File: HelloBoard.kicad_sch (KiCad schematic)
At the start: 42 parts, among them J1 USB_B_Micro, J2 Conn_01x04_Pin, J3 Conn_01x04_Pin, J4 Conn_02x08_Top_Bottom, SW1 SW_Push, SW2 SW_Push, U1 STM32F103C8T6, U2 AMS1117-3.3, U3 TMP235A2DCKR, U4 ADXL343, Y1 16MHz

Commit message: basic placement done
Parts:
- added J5: Conn_01x02, Connector_PinHeader_2.54mm:PinHeader_1x02_P2.54mm_Vertical, symbol Connector_Generic:Conn_01x02
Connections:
- net USER_LED_K: now reaches D2.1 (K), R5.2
- net at U4.8 (INT1): now also J5.1 (Pin_1)
- net at U4.9 (INT2): now also J5.2 (Pin_2)
- net NODE_USER_BUTTON: now reaches R6.1, R7.1, SW2.2
- no-connect marks 13 -> 11
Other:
- note added: "TODO: accelerometer footprint and schematic"
- note removed: "TODO: 7 Seg footprint 74HC595 for 7 seg ?"
- moved on the sheet: SW2, U4

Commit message: حلتيته
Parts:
- D1, D2: footprint LED_SMD:LED_0201_0603Metric -> LED_SMD:LED_0603_1608Metric
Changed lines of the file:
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@@
 			)
 		)
-		(property "Footprint" "LED_SMD:LED_0201_0603Metric"
+		(property "Footprint" "LED_SMD:LED_0603_1608Metric"
 			(at 99.06 179.07 0)
 			(effects
@@
 			)
 		)
-		(property "Footprint" "LED_SMD:LED_0201_0603Metric"
+		(property "Footprint" "LED_SMD:LED_0603_1608Metric"
 			(at 53.34 137.16 0)
 			(effects

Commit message: gonna try stuff, checkpoint
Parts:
- added R10, R11, R12, R13, R14, R15, R16, R8, R9: 220, Resistor_SMD:R_0402_1005Metric, symbol Device:R
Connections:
- net 7SEG_A: now also R12.1; no longer LED1.10 (A)
- net 7SEG_B: now also R11.1; no longer LED1.9 (B)
- net 7SEG_C: now also R13.1; no longer LED1.1 (C)
- net 7SEG_D: now also R15.1; no longer LED1.4 (D)
- net 7SEG_D1_CA: now also R10.1; no longer LED1.8 (DIG1)
- net 7SEG_D2_CA: now also R9.1; no longer LED1.7 (DIG2)
- net 7SEG_E: now also R14.1; no longer LED1.3 (E)
- net 7SEG_F: now also R8.1; no longer LED1.6 (F)
- net 7SEG_G: now also R16.1; no longer LED1.5 (G)
- new net A: LED1.10 (A), R12.2
- new net B: LED1.9 (B), R11.2
- new net C: LED1.1 (C), R13.2
- new net D: LED1.4 (D), R15.2
- new net D1_CA: LED1.8 (DIG1), R10.2
- new net D2_CA: LED1.7 (DIG2), R9.2
- new net E: LED1.3 (E), R14.2
- new net F: LED1.6 (F), R8.2
- new net G: LED1.5 (G), R16.2

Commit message: minor silkscreen edits
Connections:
- net ADXL_INT1: now reaches J5.1 (Pin_1), U4.8 (INT1)
- net ADXL_INT2: now reaches J5.2 (Pin_2), U4.9 (INT2)
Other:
- moved on the sheet: J5
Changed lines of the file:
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@@
 	)
 	(rectangle
-		(start 142.24 111.76)
-		(end 220.98 163.83)
+		(start 142.24 110.49)
+		(end 222.25 163.83)
 		(stroke
 			(width 0)
@@
 	(rectangle
 		(start 181.61 78.74)
-		(end 222.25 110.49)
+		(end 222.25 109.22)
 		(stroke
 			(width 0)
@@
 	(wire
 		(pts
-			(xy 266.7 144.78) (xy 270.51 144.78)
+			(xy 266.7 144.78) (xy 274.32 144.78)
 		)
 		(stroke
@@
 	(wire
 		(pts
-			(xy 266.7 147.32) (xy 270.51 147.32)
+			(xy 266.7 147.32) (xy 274.32 147.32)
 		)
 		(stroke
@@
 		)
 	)
+	(label "ADXL_INT2"
+		(at 270.51 147.32 270)
+		(effects
+			(font
+				(size 1.27 1.27)
+			)
+			(justify right bottom)
+		)
+	)
 	(label "BOOT0"
 		(at 53.34 64.77 0)
@@
 	)
 	(label "F"
-		(at 167.64 113.03 0)
+		(at 167.64 113.03 180)
 		(effects
 			(font
 				(size 1.27 1.27)
 			)
-			(justify left bottom)
+			(justify right bottom)
 		)
 	)
@@
 		)
 	)
+	(label "ADXL_INT1"
+		(at 270.51 144.78 90)
+		(effects
+			(font
+				(size 1.27 1.27)
+			)
+			(justify left bottom)
+		)
+	)
 	(label "I2C_SCL"
 		(at 35.56 179.07 0)
@@
 		(on_board yes)
 		(dnp no)
-		(fields_autoplaced yes)
 		(property "Reference" "U4"
-			(at 269.24 138.3598 0)
+			(at 264.922 129.794 0)
 			(effects
 				(font
@@
 		)
 		(property "Value" "ADXL343"
-			(at 269.24 140.8998 0)
+			(at 264.922 132.334 0)
 			(effects
 				(font
@@
 	(symbol
 		(lib_id "Connector_Generic:Conn_01x02")
-		(at 275.59 144.78 0)
+		(at 279.4 144.78 0)
 		(unit 1)
 		(exclude_from_sim no)
@@
 		(dnp no)
 		(property "Reference" "J5"
-			(at 268.478 152.654 0)
+			(at 269.494 159.004 0)
 			(effects
 				(font
@@
 		)
 		(property "Value" "Conn_01x02"
-			(at 268.478 155.194 0)
+			(at 269.494 161.544 0)
 			(effects
 				(font
@@
 		)
 		(property "Footprint" "Connector_PinHeader_2.54mm:PinHeader_1x02_P2.54mm_Vertical"
-			(at 275.59 144.78 0)
+			(at 279.4 144.78 0)
 			(effects
 				(font
@@
 		)
 		(property "Datasheet" "~"
-			(at 275.59 144.78 0)
+			(at 279.4 144.78 0)
 			(effects
 				(font
@@
 		)
 		(property "Description" "Generic connector, single row, 01x02, script generated (kicad-library-utils/schlib/autogen/connector/)"
-			(at 275.59 144.78 0)
+			(at 279.4 144.78 0)
 			(effects
 				(font

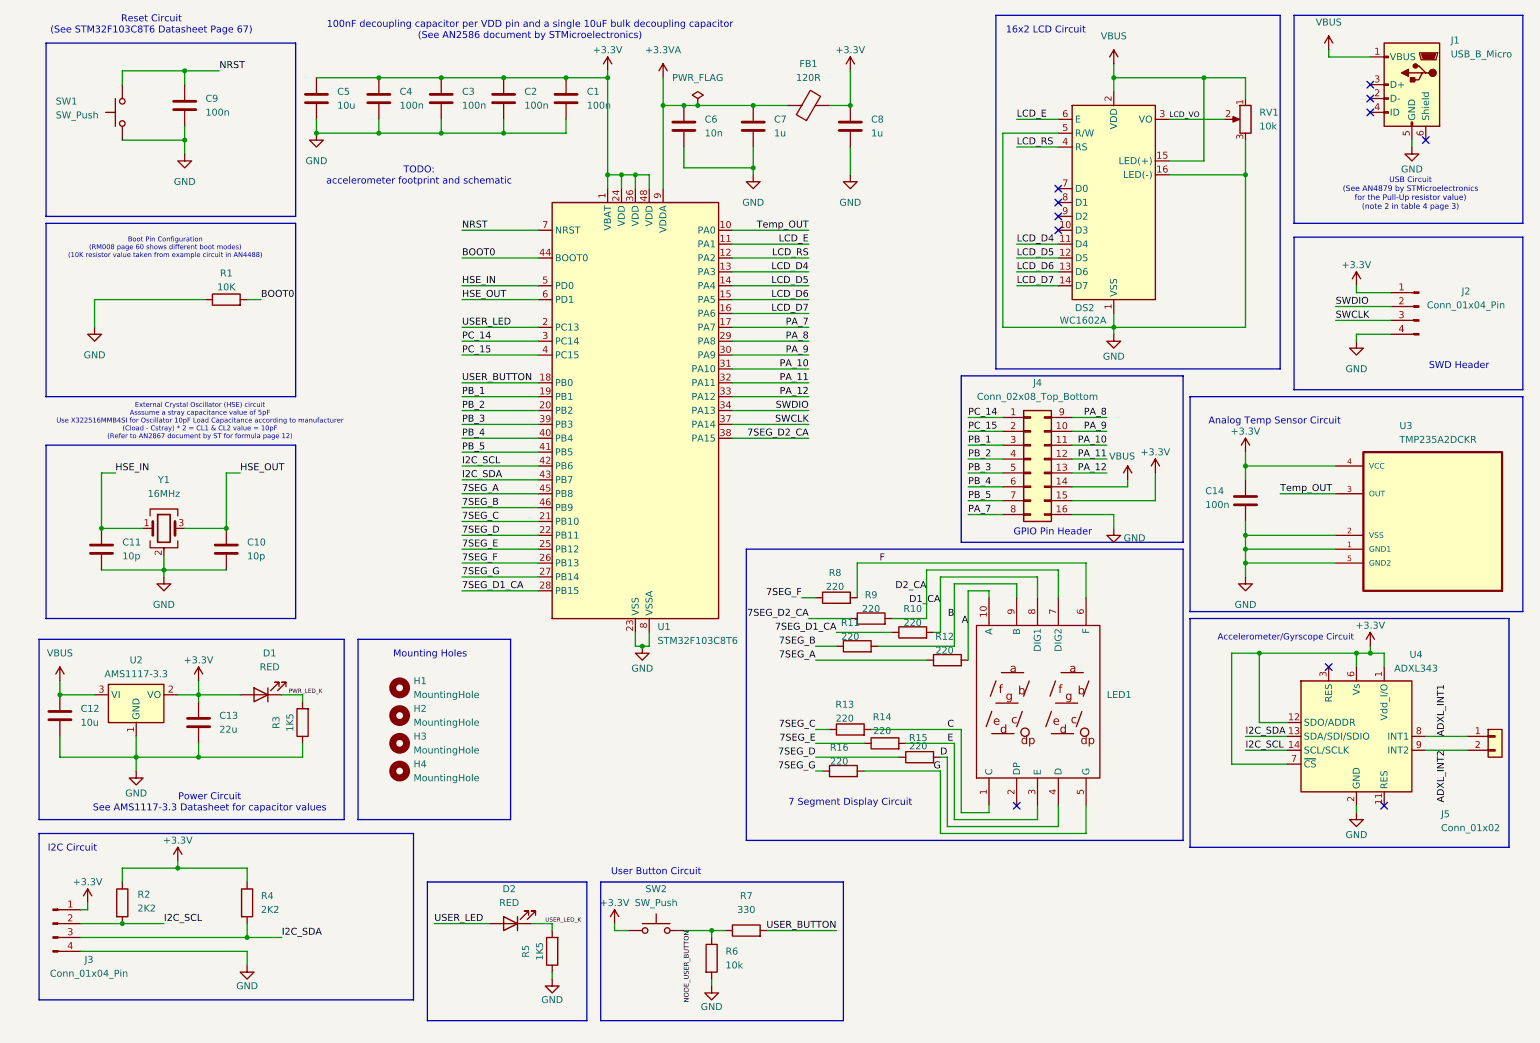
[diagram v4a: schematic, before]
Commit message: minor via edits
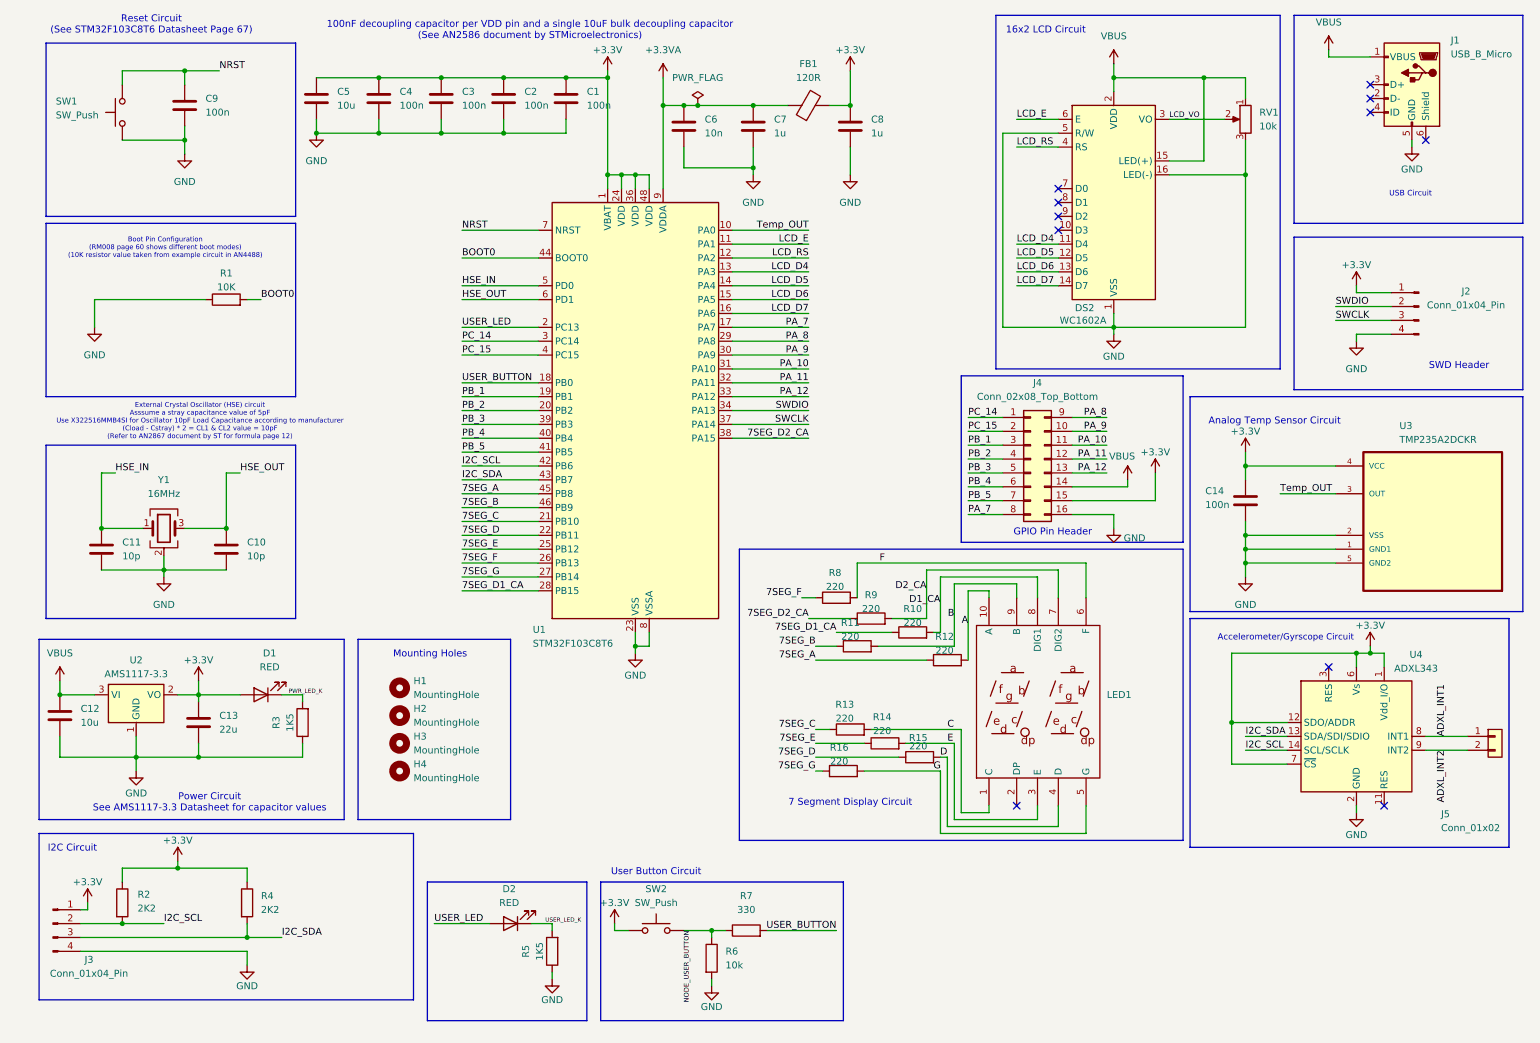
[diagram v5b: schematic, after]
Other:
- note added: "USB Circuit"
- note removed: "TODO: accelerometer footprint and schematic"
- note removed: "USB Circuit (See AN4879 by STMicroelectronics for the Pull-Up resistor value) (note 2 in table 4 page 3)"
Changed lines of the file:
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@@
 	)
 	(rectangle
-		(start 142.24 110.49)
+		(start 140.97 110.49)
 		(end 222.25 163.83)
 		(stroke
@@
 		)
 	)
-	(text "USB Circuit\n(See AN4879 by STMicroelectronics\nfor the Pull-Up resistor value)\n(note 2 in table 4 page 3)"
+	(text "USB Circuit\n"
 		(exclude_from_sim no)
 		(at 263.906 45.466 0)
@@
 		)
 	)
-	(text "TODO:\naccelerometer footprint and schematic\n\n\n"
-		(exclude_from_sim no)
-		(at 82.296 44.196 0)
-		(effects
-			(font
-				(size 1.27 1.27)
-			)
-		)
-	)
 	(text "I2C Circuit\n"
 		(exclude_from_sim no)
@@
 	)
 	(junction
-		(at 236.22 129.54)
-		(diameter 0)
-		(color 0 0 0 0)
-	)
-	(junction
 		(at 233.68 41.91)
 		(diameter 0)
@@
 	)
 	(junction
+		(at 231.14 142.24)
+		(diameter 0)
+		(color 0 0 0 0)
+	)
+	(junction
 		(at 30.48 148.59)
 		(diameter 0)
@@
 	)
 	(junction
-		(at 109.22 24.13)
+		(at 121.92 128.27)
 		(diameter 0)
 		(color 0 0 0 0)
 	)
 	(junction
-		(at 143.51 29.21)
+		(at 109.22 24.13)
 		(diameter 0)
 		(color 0 0 0 0)
 	)
 	(junction
-		(at 127 29.21)
+		(at 143.51 29.21)
 		(diameter 0)
 		(color 0 0 0 0)
 	)
 	(junction
-		(at 74.93 34.29)
+		(at 127 29.21)
 		(diameter 0)
 		(color 0 0 0 0)
 	)
 	(junction
-		(at 123.19 128.27)
+		(at 74.93 34.29)
 		(diameter 0)
 		(color 0 0 0 0)
@@
 	(wire
 		(pts
+			(xy 231.14 142.24) (xy 231.14 149.86)
+		)
+		(stroke
+			(width 0)
+			(type default)
+		)
+	)
+	(wire
+		(pts
 			(xy 35.56 114.3) (xy 35.56 115.57)
 		)
@@
 	(wire
 		(pts
-			(xy 241.3 142.24) (xy 236.22 142.24)
-		)
-		(stroke
-			(width 0)
-			(type default)
-		)
-	)
-	(wire
-		(pts
 			(xy 41.91 148.59) (xy 60.96 148.59)
 		)
@@
 	(wire
 		(pts
-			(xy 121.92 128.27) (xy 123.19 128.27)
+			(xy 121.92 128.27) (xy 124.46 128.27)
 		)
 		(stroke
@@
 	(wire
 		(pts
-			(xy 231.14 129.54) (xy 231.14 149.86)
-		)
-		(stroke
-			(width 0)
-			(type default)
-		)
-	)
-	(wire
-		(pts
 			(xy 266.7 144.78) (xy 274.32 144.78)
 		)
@@
 	(wire
 		(pts
-			(xy 186.69 119.38) (xy 186.69 118.11)
+			(xy 231.14 129.54) (xy 231.14 142.24)
 		)
 		(stroke
@@
 	(wire
 		(pts
-			(xy 63.5 24.13) (xy 74.93 24.13)
+			(xy 186.69 119.38) (xy 186.69 118.11)
 		)
 		(stroke
@@
 	(wire
 		(pts
-			(xy 154.94 146.05) (xy 163.83 146.05)
+			(xy 63.5 24.13) (xy 74.93 24.13)
 		)
 		(stroke
@@
 	(wire
 		(pts
-			(xy 163.83 151.13) (xy 177.8 151.13)
+			(xy 154.94 146.05) (xy 163.83 146.05)
 		)
 		(stroke
@@
 	(wire
 		(pts
-			(xy 30.48 144.78) (xy 30.48 148.59)
+			(xy 163.83 151.13) (xy 177.8 151.13)
 		)
 		(stroke
@@
 	(wire
 		(pts
-			(xy 143.51 36.83) (xy 143.51 40.64)
+			(xy 30.48 144.78) (xy 30.48 148.59)
 		)
 		(stroke
@@
 	(wire
 		(pts
-			(xy 236.22 129.54) (xy 236.22 142.24)
+			(xy 143.51 36.83) (xy 143.51 40.64)
 		)
 		(stroke
@@
 	(wire
 		(pts
+			(xy 231.14 142.24) (xy 241.3 142.24)
+		)
+		(stroke
+			(width 0)
+			(type default)
+		)
+	)
+	(wire
+		(pts
 			(xy 180.34 160.02) (xy 180.34 146.05)
 		)
@@
 	(wire
 		(pts
-			(xy 231.14 129.54) (xy 236.22 129.54)
-		)
-		(stroke
-			(width 0)
-			(type default)
-		)
-	)
-	(wire
-		(pts
 			(xy 86.36 34.29) (xy 97.79 34.29)
 		)
@@
 	(wire
 		(pts
-			(xy 236.22 129.54) (xy 254 129.54)
+			(xy 231.14 129.54) (xy 254 129.54)
 		)
 		(stroke
@@
 	(wire
 		(pts
-			(xy 123.19 128.27) (xy 124.46 128.27)
+			(xy 209.55 104.14) (xy 209.55 106.68)
 		)
 		(stroke
@@
 	(wire
 		(pts
-			(xy 209.55 104.14) (xy 209.55 106.68)
+			(xy 201.93 91.44) (xy 208.28 91.44)
 		)
 		(stroke
@@
 	(wire
 		(pts
-			(xy 201.93 91.44) (xy 208.28 91.44)
+			(xy 121.92 129.54) (xy 121.92 128.27)
 		)
 		(stroke
@@
 	(symbol
 		(lib_id "power:GND")
-		(at 123.19 128.27 0)
+		(at 121.92 129.54 0)
 		(unit 1)
 		(exclude_from_sim no)
@@
 		(dnp no)
 		(property "Reference" "#PWR01"
-			(at 123.19 134.62 0)
+			(at 121.92 135.89 0)
 			(effects
 				(font
@@
 		)
 		(property "Value" "GND"
-			(at 123.19 132.334 0)
+			(at 121.92 133.604 0)
 			(effects
 				(font
@@
 		)
 		(property "Footprint" ""
-			(at 123.19 128.27 0)
+			(at 121.92 129.54 0)
 			(effects
 				(font
@@
 		)
 		(property "Datasheet" ""
-			(at 123.19 128.27 0)
+			(at 121.92 129.54 0)
 			(effects
 				(font
@@
 		)
 		(property "Description" "Power symbol creates a global label with name \"GND\" , ground"
-			(at 123.19 128.27 0)
+			(at 121.92 129.54 0)
 			(effects
 				(font
@@
 		(dnp no)
 		(property "Reference" "U1"
-			(at 125.984 124.714 0)
+			(at 103.124 125.222 0)
 			(effects
 				(font
@@
 		)
 		(property "Value" "STM32F103C8T6"
-			(at 125.984 127.254 0)
+			(at 103.124 127.762 0)
 			(effects
 				(font

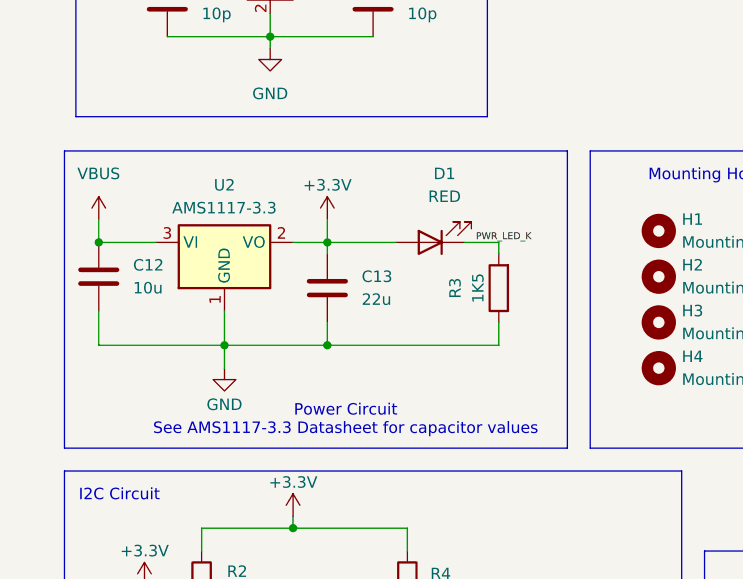
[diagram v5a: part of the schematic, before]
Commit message: stuck with the ams1117-3.3
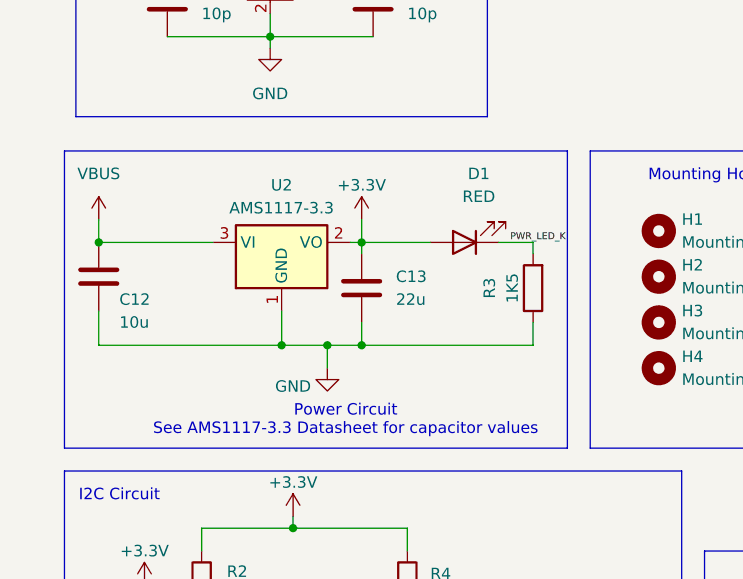
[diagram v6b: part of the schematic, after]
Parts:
- C13: footprint Capacitor_Tantalum_SMD:CP_EIA-6032-15_Kemet-U -> Capacitor_Tantalum_SMD:CP_EIA-3528-21_Kemet-B
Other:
- moved on the sheet: C13, D1, R3, U2
